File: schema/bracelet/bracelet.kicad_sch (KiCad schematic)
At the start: 8 parts, among them J1 POGO_PIN_F, J2 Battery_soldering_pads, J3 BMI_270, U1 ESP32-C3-WROOM-02, U3 MCP1700x-330xxTO

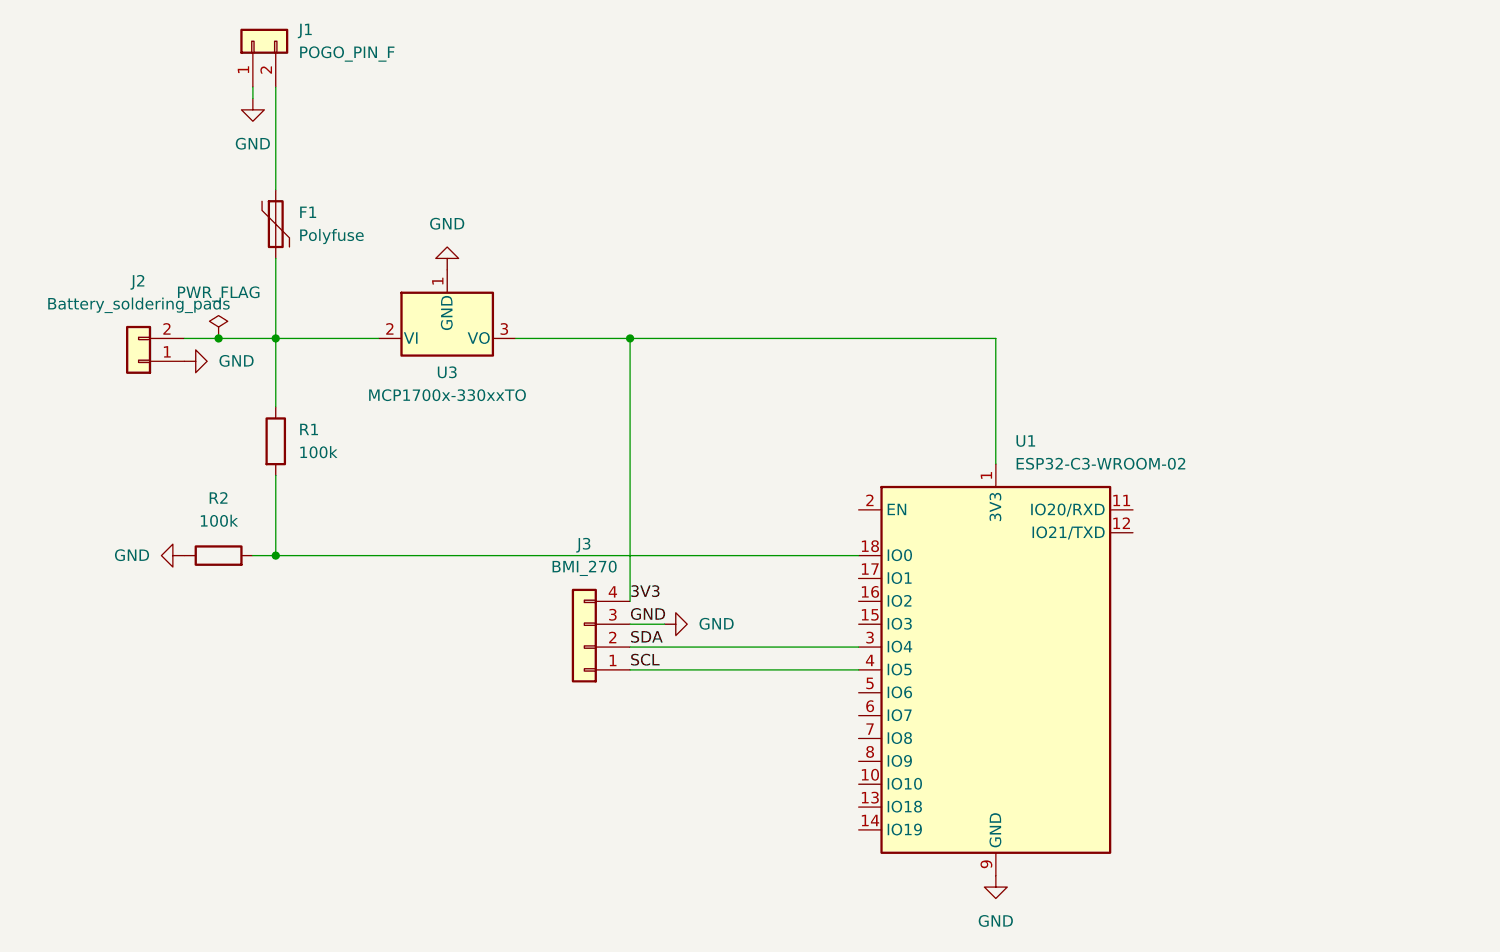
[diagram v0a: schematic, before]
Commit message: Design bracelet PCB
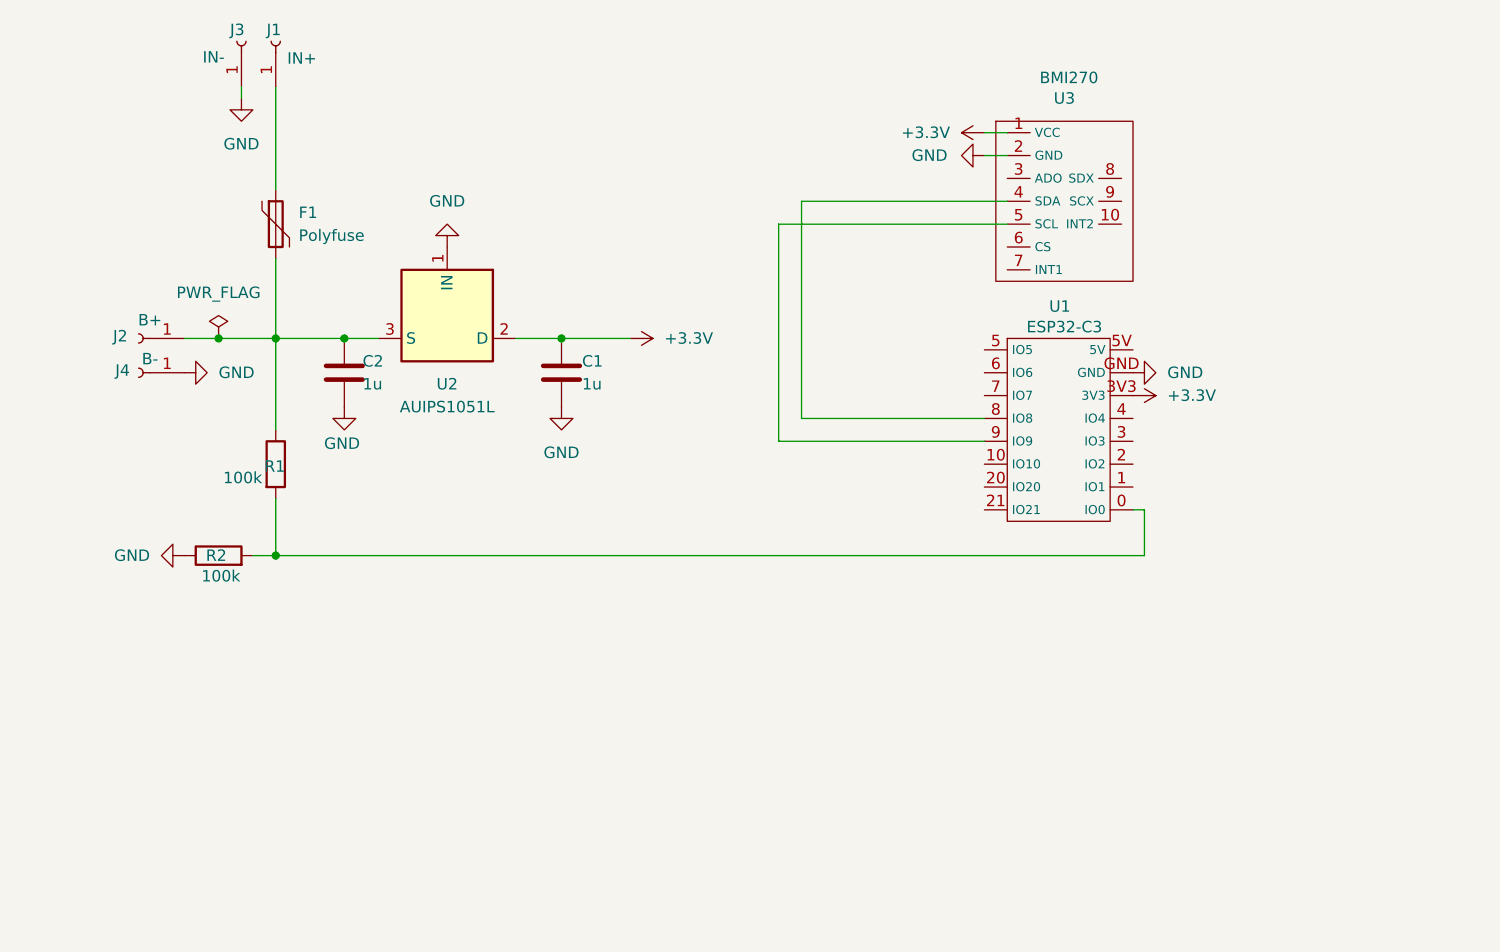
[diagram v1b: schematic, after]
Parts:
- removed J1: POGO_PIN_F, symbol Connector_Generic:Conn_01x02
- removed J2: Battery_soldering_pads, Connector_PinHeader_2.54mm:PinHeader_1x02_P2.54mm_Horizontal, symbol Connector_Generic:Conn_01x02
- removed J3: BMI_270, symbol Connector_Generic:Conn_01x04
- removed U1: ESP32-C3-WROOM-02, RF_Module:ESP32-C3-WROOM-02, symbol RF_Module:ESP32-C3-WROOM-02
- removed U3: MCP1700x-330xxTO, Package_TO_SOT_THT:TO-92_Inline, symbol Regulator_Linear:MCP1700x-330xxTO
- added C1, C2: 1u, Capacitor_SMD:C_0805_2012Metric, symbol Device:C
- added J1: IN+, Connector_Wire:SolderWirePad_1x01_SMD_2x4mm, symbol Connector:Conn_01x01_Socket
- added J2: B+, Connector_Wire:SolderWirePad_1x01_SMD_2x4mm, symbol Connector:Conn_01x01_Socket
- added J3: IN-, Connector_Wire:SolderWirePad_1x01_SMD_2x4mm, symbol Connector:Conn_01x01_Socket
- added J4: B-, Connector_Wire:SolderWirePad_1x01_SMD_2x4mm, symbol Connector:Conn_01x01_Socket
- added U1: ESP32-C3, Library_Perso:ESP32-C3 HW-466B, symbol Library_Perso:ESP32-c3-hw-466b
- added U2: AUIPS1051L, Package_TO_SOT_SMD:SOT-223-3_TabPin2, symbol Power_Management:AUIPS1051L
- added U3: BMI270, Library_Perso:BMI270 module, symbol Library_Perso:BMI270
- F1: footprint (none) -> Capacitor_THT:C_Disc_D5.0mm_W2.5mm_P5.00mm
- R1, R2: footprint (none) -> Resistor_SMD:R_1206_3216Metric
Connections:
- net GND: now also C1.2, C2.2, J3.1 (Pin_1), J4.1 (Pin_1), U1.GND, U2.1 (IN), U3.2 (GND)
- net at F1.2, R1.1: now also C2.1, J2.1 (Pin_1), U2.3 (S)
- net at R1.2, R2.2: now also U1.0 (IO0)
- net at F1.1: now also J1.1 (Pin_1)
- new net: U1.8 (IO8), U3.4 (SDA)
- new net: U1.9 (IO9), U3.5 (SCL)
- new net +3.3V: C1.1, U1.3V3, U2.2 (D), U3.1 (VCC)
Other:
- moved on the sheet: R1

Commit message: Update Architecture db
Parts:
- added D1: 1N5819, Diode_SMD:D_SMA, symbol Diode:1N5819
- added J5: Vib+, Connector_Wire:SolderWirePad_1x01_SMD_2x4mm, symbol Connector:Conn_01x01_Socket
- added J6: Vib-, Connector_Wire:SolderWirePad_1x01_SMD_2x4mm, symbol Connector:Conn_01x01_Socket
- added Q1: AO3400A, Package_TO_SOT_SMD:SOT-23, symbol Transistor_FET:AO3400A
- added R3: 100, Resistor_SMD:R_1206_3216Metric, symbol Device:R
- added R4: 100k, Resistor_SMD:R_1206_3216Metric, symbol Device:R
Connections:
- net +3.3V: now also D1.1 (K), J5.1 (Pin_1)
- net GND: now also Q1.2 (S), R4.2
- net at R1.2, R2.2: now also U1.1 (IO1); no longer U1.0 (IO0)
- net at U1.2 (IO2): now also U3.5 (SCL)
- net at U1.3 (IO3): now also U3.4 (SDA)
- net at U1.8 (IO8): no longer U3.4 (SDA)
- net at U1.9 (IO9): no longer U3.5 (SCL)
- new net: Q1.1 (G), R3.2, R4.1
- new net: R3.1, U1.0 (IO0)
- new net: D1.2 (A), J6.1 (Pin_1), Q1.3 (D)
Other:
- moved on the sheet: U1, U3
